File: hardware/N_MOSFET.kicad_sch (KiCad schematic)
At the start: 4 parts, among them Q1 Q_NMOS_DGS

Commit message: jolo
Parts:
- renumbered Q1 to Q4, R21 to R31, R22 to R32, R23 to R33
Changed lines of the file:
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@@
   (symbol (lib_id "Device:Q_NMOS_DGS") (at 161.29 102.87 0)
     (in_bom yes) (on_board yes)
-    (property "Reference" "Q1" (id 0) (at 170.18 104.14 90)
+    (property "Reference" "Q4" (id 0) (at 170.18 104.14 90)
       (effects (font (size 1.27 1.27)) (justify left))
     )
@@
   (symbol (lib_id "Device:R_Small") (at 153.67 107.95 0) (mirror y)
     (in_bom yes) (on_board yes)
-    (property "Reference" "R22" (id 0) (at 151.13 107.95 90)
+    (property "Reference" "R32" (id 0) (at 151.13 107.95 90)
       (effects (font (size 1.27 1.27)) (justify left))
     )
@@
   (symbol (lib_id "Device:R_Small") (at 148.59 102.87 90) (mirror x)
     (in_bom yes) (on_board yes)
-    (property "Reference" "R21" (id 0) (at 148.59 105.41 90)
+    (property "Reference" "R31" (id 0) (at 148.59 105.41 90)
       (effects (font (size 1.27 1.27)) (justify left))
     )
@@
   (symbol (lib_id "Device:R_Small") (at 163.83 92.71 0) (mirror y)
     (in_bom yes) (on_board yes)
-    (property "Reference" "R23" (id 0) (at 161.29 92.71 90)
+    (property "Reference" "R33" (id 0) (at 161.29 92.71 90)
       (effects (font (size 1.27 1.27)) (justify left))
     )
@@
   (symbol (lib_id "power:GND") (at 163.83 115.57 0) (mirror y)
     (in_bom yes) (on_board yes)
-    (property "Reference" "#PWR0106" (id 0) (at 163.83 121.92 0)
+    (property "Reference" "#PWR0107" (id 0) (at 163.83 121.92 0)
       (effects (font (size 1.27 1.27)) hide)
     )

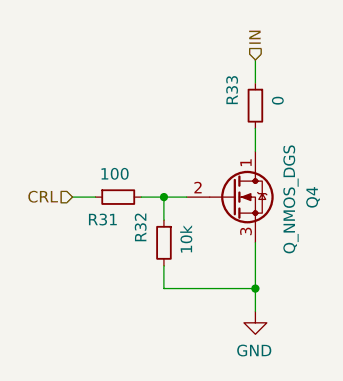
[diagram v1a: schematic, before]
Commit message: major schematic update, changed optocouplers for different, added new fuses for 5v supply for water and potentiometers and 24v supply for BSPD/ESB, updated autosport connector, and some other changes
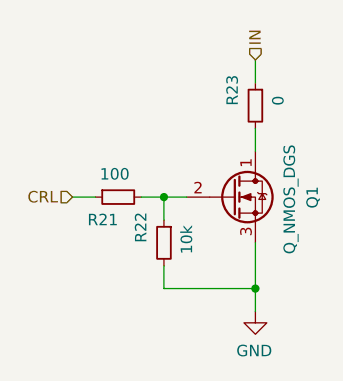
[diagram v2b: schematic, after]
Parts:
- renumbered Q4 to Q1, R31 to R21, R32 to R22, R33 to R23
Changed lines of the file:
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@@
   (symbol (lib_id "Device:Q_NMOS_DGS") (at 161.29 102.87 0)
     (in_bom yes) (on_board yes)
-    (property "Reference" "Q4" (id 0) (at 170.18 104.14 90)
+    (property "Reference" "Q1" (id 0) (at 170.18 104.14 90)
       (effects (font (size 1.27 1.27)) (justify left))
     )
@@
   (symbol (lib_id "Device:R_Small") (at 153.67 107.95 0) (mirror y)
     (in_bom yes) (on_board yes)
-    (property "Reference" "R32" (id 0) (at 151.13 107.95 90)
+    (property "Reference" "R22" (id 0) (at 151.13 107.95 90)
       (effects (font (size 1.27 1.27)) (justify left))
     )
@@
   (symbol (lib_id "Device:R_Small") (at 148.59 102.87 90) (mirror x)
     (in_bom yes) (on_board yes)
-    (property "Reference" "R31" (id 0) (at 148.59 105.41 90)
+    (property "Reference" "R21" (id 0) (at 148.59 105.41 90)
       (effects (font (size 1.27 1.27)) (justify left))
     )
@@
   (symbol (lib_id "Device:R_Small") (at 163.83 92.71 0) (mirror y)
     (in_bom yes) (on_board yes)
-    (property "Reference" "R33" (id 0) (at 161.29 92.71 90)
+    (property "Reference" "R23" (id 0) (at 161.29 92.71 90)
       (effects (font (size 1.27 1.27)) (justify left))
     )
@@
   (symbol (lib_id "power:GND") (at 163.83 115.57 0) (mirror y)
     (in_bom yes) (on_board yes)
-    (property "Reference" "#PWR0107" (id 0) (at 163.83 121.92 0)
+    (property "Reference" "#PWR0106" (id 0) (at 163.83 121.92 0)
       (effects (font (size 1.27 1.27)) hide)
     )
